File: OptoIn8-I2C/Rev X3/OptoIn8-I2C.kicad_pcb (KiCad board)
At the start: 2 copper layers, 95 x 95 mm, 46 parts, among them J1 CONN_3, J2 CONN_4, J3 CONN_4, J4 CONN_3X2, J5 CONN_01X02, J6 CONN_3, J7 CONN_02X02, J8 DB25, U1 4N26, U10 MCP23008P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

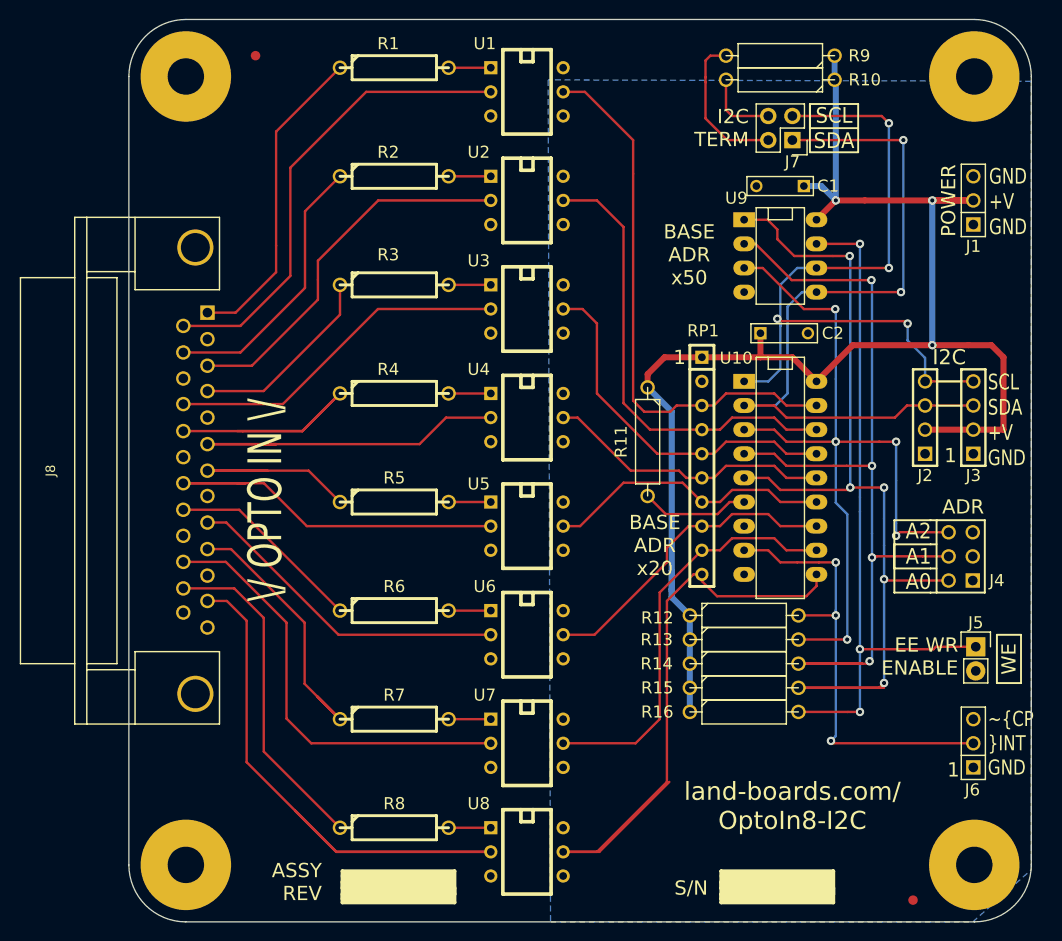
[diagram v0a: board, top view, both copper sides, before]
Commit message: Fix the DB-25 mounting holes
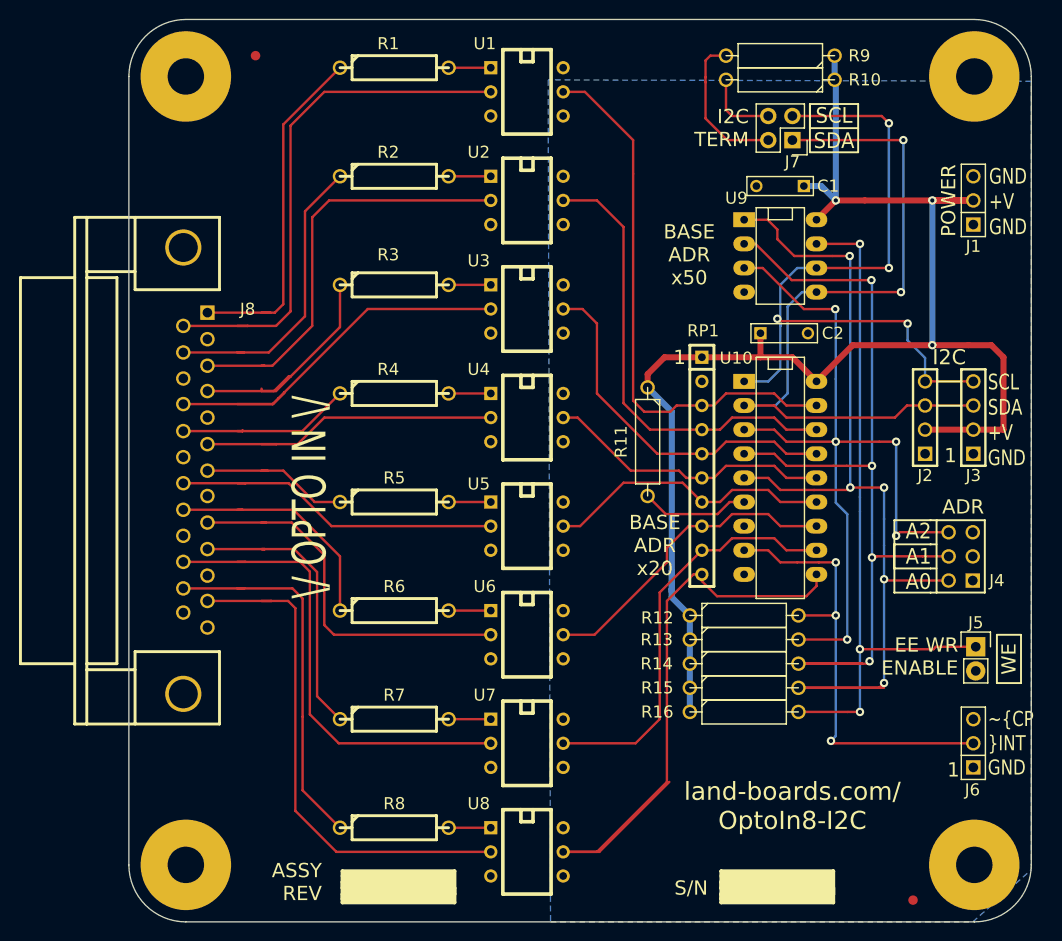
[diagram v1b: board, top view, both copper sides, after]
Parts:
- J8: footprint DougsNewMods:DB25MC -> DB25MC
- R1, R2, R3, R4, R5, R6, R7, R8: value 330 -> R
- R11, R12, R13, R14, R15: value 10K -> R
- RP1: value 4.7K-PACK -> RR9
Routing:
- net Net-(J8-Pad12): track 78.0 -> 54.3 mm
- net /CH4-IN+: track 30.7 -> 18.9 mm
- net /CH4-IN-: track 39.8 -> 32.5 mm
- net /CH5-IN-: track 41.6 -> 35.1 mm
- net /CH5-IN+: track 22.4 -> 16.1 mm
- net /CH1-IN-: track 49.3 -> 55.1 mm
- net /CH3-IN-: track 36.5 -> 42.0 mm
- net Net-(J8-Pad9): track 34.7 -> 39.5 mm
- net /CH3-IN+: track 20.4 -> 25.2 mm
- net /CH2-IN-: track 39.4 -> 44.0 mm
- net Net-(J8-Pad24): track 35.2 -> 39.5 mm
- net Net-(J8-Pad21): track 21.5 -> 25.4 mm
- net Net-(J8-Pad23): track 46.2 -> 49.9 mm
- net /CH1-IN+: track 33.3 -> 36.6 mm
- net /CH2-IN+: track 28.9 -> 31.3 mm
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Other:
- board text added: "land-boards.com/ OptoIn8-I2C PWB Rev X3"
- board text removed: "land-boards.com/ OptoIn8-I2C PWB Rev X4"
